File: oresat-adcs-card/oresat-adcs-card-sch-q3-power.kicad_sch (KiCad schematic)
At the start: 86 parts, among them Q31 MOSFET-PCH-SOT23-6, Q32 MOSFET-PCH-SOT23-6, Q33 PMV45EN2R, Q34 PMV45EN2R, U25 MAX7310ATE, U26 MAX4211FETE, U27 MIC842LYC5-TR, U28 MIC842LYC5-TR

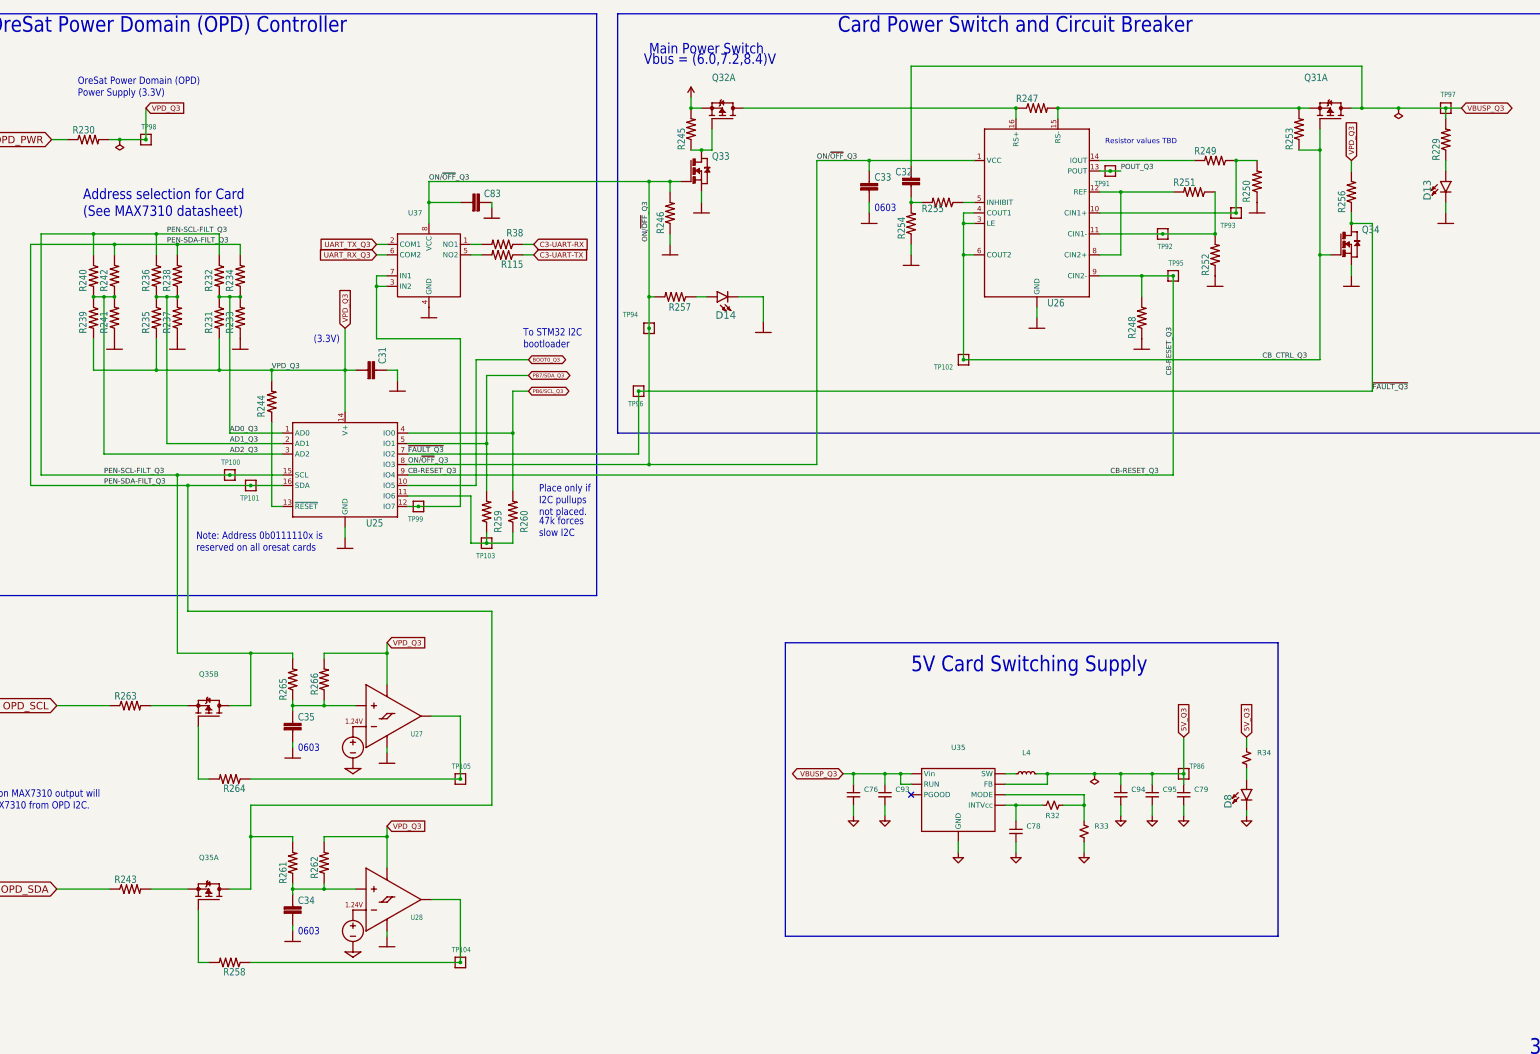
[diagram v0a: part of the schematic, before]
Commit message: Design review changes
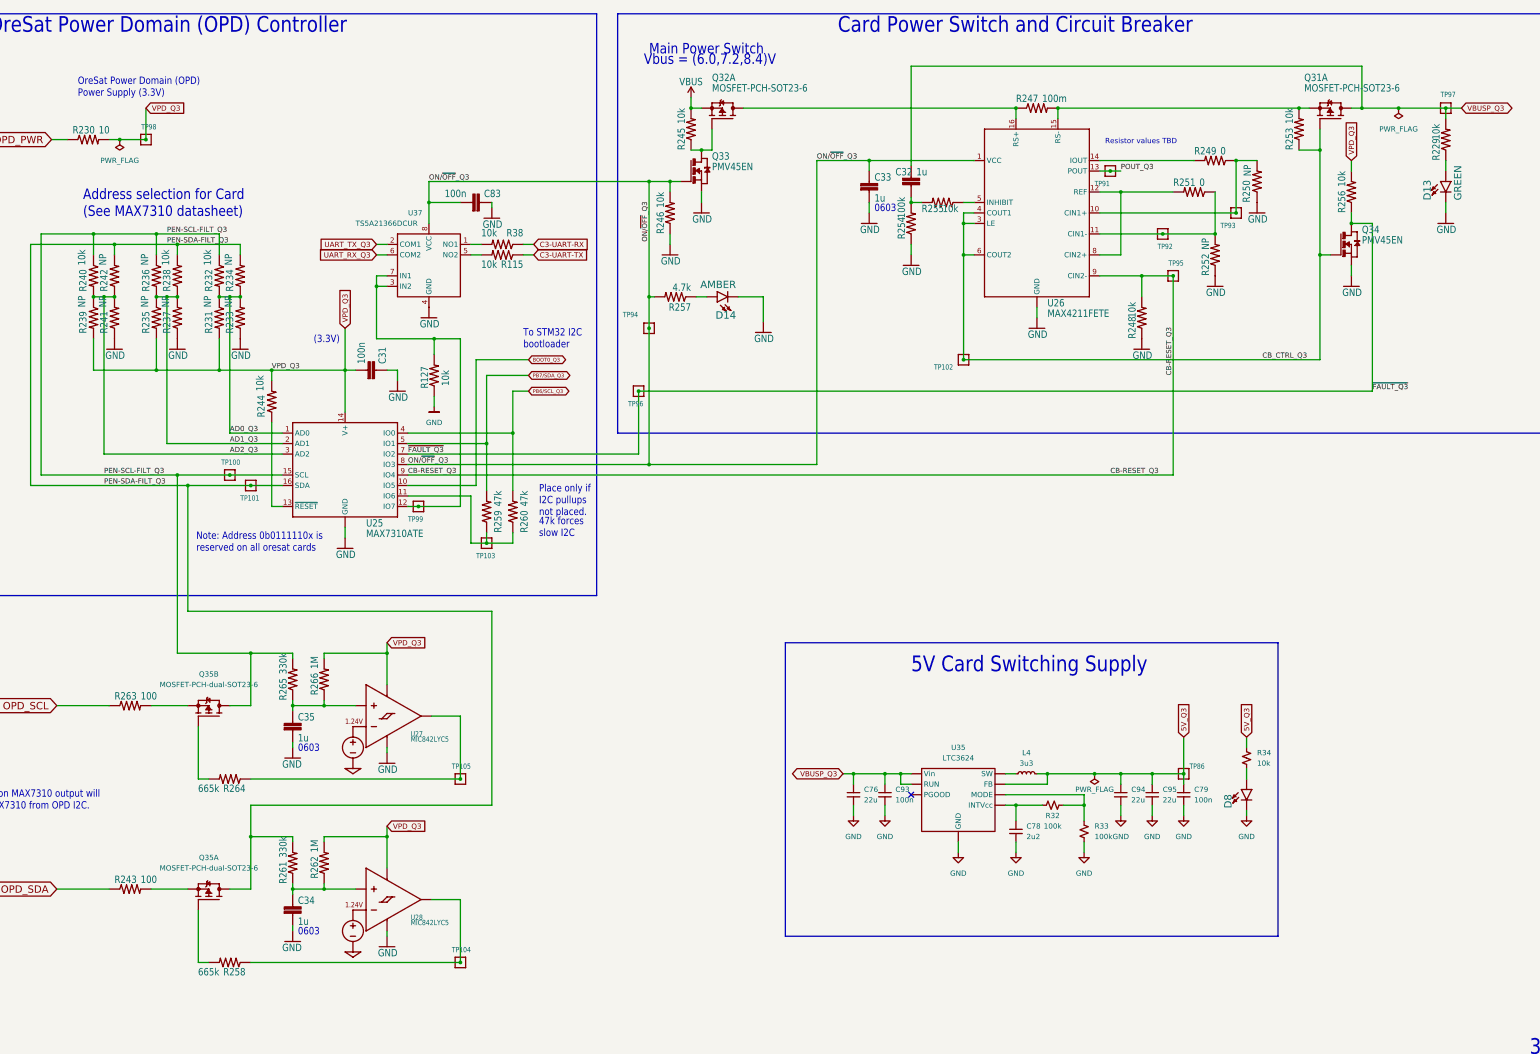
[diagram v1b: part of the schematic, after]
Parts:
- added R127: CRGCQ0603F2K7, oresat-acs-card:.0603-C-NOSILK, symbol oresat-acs-card-eagle-import:R-US_0603-C-NOSILK
- C31, C33, C34, C35, C83, R115, R229, R230, R231, R232, R233, R234, R235, R236, R237, R238, R239, R240, R241, R242, R243, R244, R245, R246, R248, R249, R250, R251, R252, R253, R254, R255, R256, R257, R258, R259, R260, R261, R262, R263, R264, R265, R266, R38: footprint (none) -> oresat-acs-card:.0603-C-NOSILK
- C32: value (none) -> 1u; footprint (none) -> oresat-acs-card:.0603-C-NOSILK
- C76, C94, C95: value (none) -> 22u; footprint (none) -> Capacitor_SMD:C_1210_3225Metric
- C78: value (none) -> 2u2; footprint (none) -> Capacitor_SMD:C_0603_1608Metric
- C79, C93: value (none) -> 100n; footprint (none) -> Capacitor_SMD:C_0603_1608Metric
- D13, D14, D8: footprint (none) -> oresat-acs-card:LED-0603
- L4: value (none) -> 3u3; footprint (none) -> Inductor_SMD:L_Coilcraft_XxL4030
- Q31, Q32: footprint (none) -> oresat-acs-card:SOT23-6
- Q33, Q34: footprint (none) -> oresat-acs-card:SOT23
- Q35: value (none) -> MOSFET-PCH-dual-SOT23-6; footprint (none) -> oresat-acs-card:SOT23-6
- R247: footprint (none) -> oresat-acs-card:R1206
- R32, R33: value (none) -> 100k; footprint (none) -> Resistor_SMD:R_0603_1608Metric
- R34: value (none) -> 10k; footprint (none) -> Resistor_SMD:R_0603_1608Metric
- TP100, TP101, TP102, TP103, TP104, TP105, TP86, TP91, TP92, TP93, TP94, TP95, TP96, TP97, TP98, TP99: value (none) -> TEST-POINT-LARGE-SQUARE; footprint (none) -> oresat-acs-card:1X01
- U25, U26: footprint (none) -> oresat-acs-card:QFN65P400X400X80-17T210
- U27, U28: footprint (none) -> oresat-acs-card:SC70-5
- U35: value (none) -> LTC3624; footprint (none) -> oresat-footprints:DFN-8-1EP_3x3mm_P0.5mm_EP1.65x2.38mm_ThermalVias0.3mm
- U37: value (none) -> TS5A21366DCUR; footprint (none) -> oresat-acs-card:DCU-R-PDSO-G8
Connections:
- net GND: now also R127.1
- net at TP99.1, U25.12 (IO7), U37.3 (IN2)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: now also R127.2

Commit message: Updated inductor footprint
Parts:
- L4: footprint Inductor_SMD:L_Coilcraft_XxL4030 -> oresat-footprints:L_ECS-MPI4040
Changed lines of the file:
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@@
     (property "Reference" "L4" (id 0) (at 285.75 193.04 90))
     (property "Value" "3u3" (id 1) (at 285.75 195.58 90))
-    (property "Footprint" "Inductor_SMD:L_Coilcraft_XxL4030" (id 2) (at 285.75 198.12 0)
+    (property "Footprint" "oresat-footprints:L_ECS-MPI4040" (id 2) (at 285.75 198.12 0)
       (effects (font (size 1.27 1.27)) hide)
     )

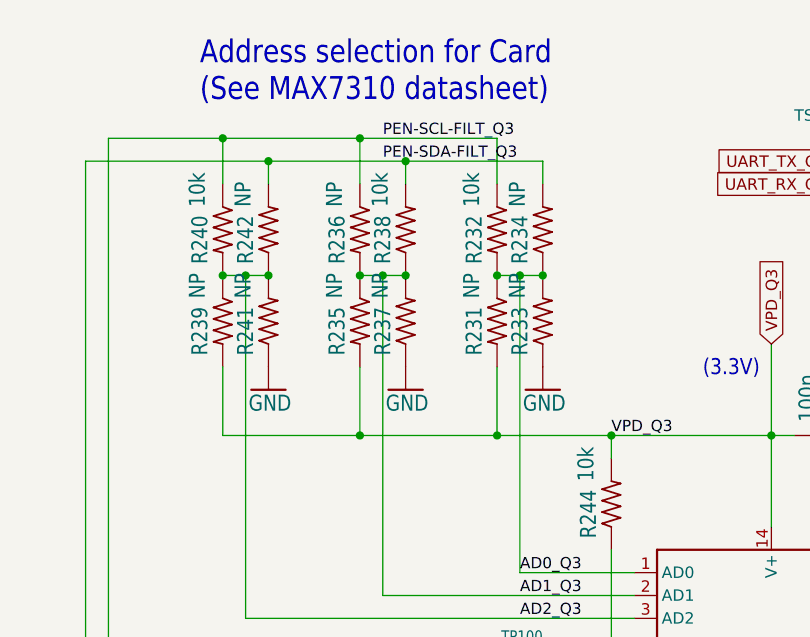
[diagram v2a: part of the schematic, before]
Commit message: Updated MT OPD breaker current limiting, and added OPD addresses to schematic
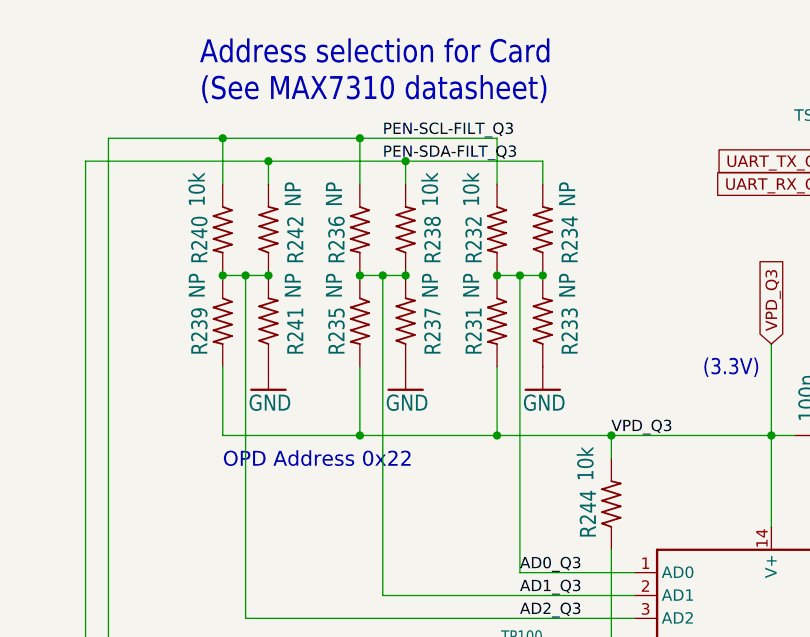
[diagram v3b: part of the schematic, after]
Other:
- note added: "OPD Address 0x22"
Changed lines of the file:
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@@
     (effects (font (size 1.778 1.5113)) (justify left bottom))
+  )
+  (text "OPD Address 0x22" (at 59.69 104.14 0)
+    (effects (font (size 1.651 1.651)) (justify left bottom))
   )
   (text "0603" (at 109.22 193.04 180)
@@
   (symbol (lib_id "oresat-acs-card-eagle-import:R-US_0603-C-NOSILK") (at 64.77 77.47 90) (unit 1)
     (in_bom yes) (on_board yes)
-    (property "Reference" "R242" (id 0) (at 63.2714 81.28 0)
-      (effects (font (size 1.778 1.5113)) (justify left bottom))
-    )
-    (property "Value" "NP" (id 1) (at 62.992 74.93 0)
+    (property "Reference" "R242" (id 0) (at 68.8594 81.28 0)
+      (effects (font (size 1.778 1.5113)) (justify left bottom))
+    )
+    (property "Value" "NP" (id 1) (at 68.58 74.93 0)
       (effects (font (size 1.778 1.5113)) (justify left bottom))
     )
@@
   (symbol (lib_id "oresat-acs-card-eagle-import:R-US_0603-C-NOSILK") (at 95.25 77.47 90) (unit 1)
     (in_bom yes) (on_board yes)
-    (property "Reference" "R234" (id 0) (at 93.7514 81.28 0)
-      (effects (font (size 1.778 1.5113)) (justify left bottom))
-    )
-    (property "Value" "NP" (id 1) (at 93.472 74.93 0)
+    (property "Reference" "R234" (id 0) (at 99.3394 81.28 0)
+      (effects (font (size 1.778 1.5113)) (justify left bottom))
+    )
+    (property "Value" "NP" (id 1) (at 99.06 74.93 0)
       (effects (font (size 1.778 1.5113)) (justify left bottom))
     )
@@
   (symbol (lib_id "oresat-acs-card-eagle-import:R-US_0603-C-NOSILK") (at 80.01 87.63 90) (unit 1)
     (in_bom yes) (on_board yes)
-    (property "Reference" "R237" (id 0) (at 78.5114 91.44 0)
-      (effects (font (size 1.778 1.5113)) (justify left bottom))
-    )
-    (property "Value" "NP" (id 1) (at 78.232 85.09 0)
+    (property "Reference" "R237" (id 0) (at 84.0994 91.44 0)
+      (effects (font (size 1.778 1.5113)) (justify left bottom))
+    )
+    (property "Value" "NP" (id 1) (at 83.82 85.09 0)
       (effects (font (size 1.778 1.5113)) (justify left bottom))
     )
@@
   (symbol (lib_id "oresat-acs-card-eagle-import:R-US_0603-C-NOSILK") (at 64.77 87.63 90) (unit 1)
     (in_bom yes) (on_board yes)
-    (property "Reference" "R241" (id 0) (at 63.2714 91.44 0)
-      (effects (font (size 1.778 1.5113)) (justify left bottom))
-    )
-    (property "Value" "NP" (id 1) (at 62.992 85.09 0)
+    (property "Reference" "R241" (id 0) (at 68.8594 91.44 0)
+      (effects (font (size 1.778 1.5113)) (justify left bottom))
+    )
+    (property "Value" "NP" (id 1) (at 68.58 85.09 0)
       (effects (font (size 1.778 1.5113)) (justify left bottom))
     )
@@
   (symbol (lib_id "oresat-acs-card-eagle-import:R-US_0603-C-NOSILK") (at 95.25 87.63 90) (unit 1)
     (in_bom yes) (on_board yes)
-    (property "Reference" "R233" (id 0) (at 93.7514 91.44 0)
-      (effects (font (size 1.778 1.5113)) (justify left bottom))
-    )
-    (property "Value" "NP" (id 1) (at 93.472 85.09 0)
+    (property "Reference" "R233" (id 0) (at 99.3394 91.44 0)
+      (effects (font (size 1.778 1.5113)) (justify left bottom))
+    )
+    (property "Value" "NP" (id 1) (at 99.06 85.09 0)
       (effects (font (size 1.778 1.5113)) (justify left bottom))
     )
@@
   (symbol (lib_id "oresat-acs-card-eagle-import:R-US_0603-C-NOSILK") (at 80.01 77.47 90) (unit 1)
     (in_bom yes) (on_board yes)
-    (property "Reference" "R238" (id 0) (at 78.5114 81.28 0)
-      (effects (font (size 1.778 1.5113)) (justify left bottom))
-    )
-    (property "Value" "10k" (id 1) (at 78.232 74.93 0)
-      (effects (font (size 1.778 1.5113)) (justify left bottom))
-    )
+    (property "Reference" "R238" (id 0) (at 84.0994 81.28 0)
+      (effects (font (size 1.778 1.5113)) (justify left bottom))
+    )
+    (property "Value" "10k" (id 1) (at 83.82 74.93 0)
+      (effects (font (size 1.778 1.5113)) (justify left bottom))
+    )

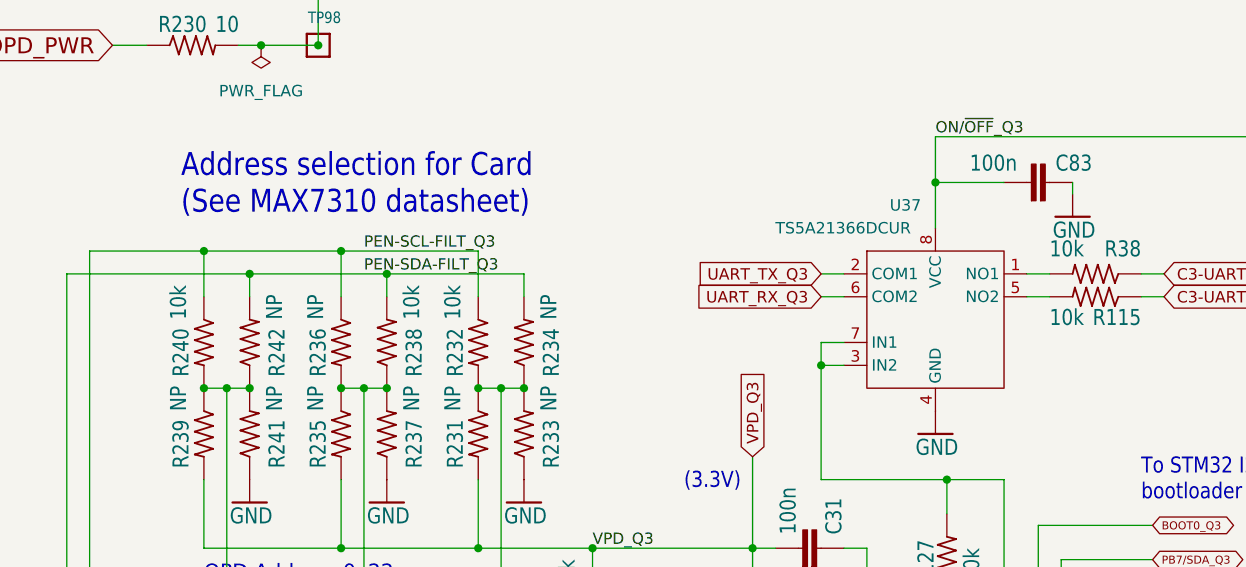
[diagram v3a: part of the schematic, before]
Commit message: Fixed ADCS card issues
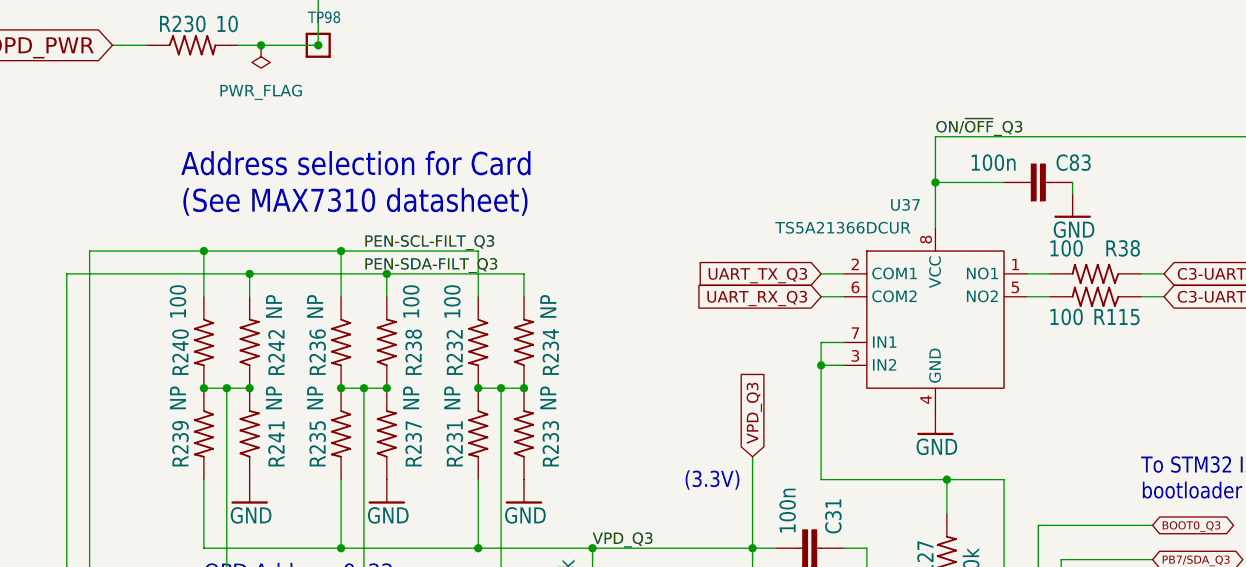
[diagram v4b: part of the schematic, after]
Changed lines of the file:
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@@
       (effects (font (size 1.778 1.5113)) (justify left bottom))
     )
-    (property "Value" "10k" (id 1) (at 157.48 73.66 0)
+    (property "Value" "100" (id 1) (at 157.48 73.66 0)
       (effects (font (size 1.778 1.5113)) (justify left bottom))
     )
@@
       (effects (font (size 1.778 1.5113)) (justify left bottom))
     )
-    (property "Value" "10k" (id 1) (at 157.48 66.04 0)
+    (property "Value" "100" (id 1) (at 157.48 66.04 0)
       (effects (font (size 1.778 1.5113)) (justify left bottom))
     )
@@
       (effects (font (size 1.778 1.5113)) (justify left bottom))
     )
-    (property "Value" "10k" (id 1) (at 83.82 74.93 0)
+    (property "Value" "100" (id 1) (at 83.82 74.93 0)
       (effects (font (size 1.778 1.5113)) (justify left bottom))
     )
@@
       (effects (font (size 1.778 1.5113)) (justify right top))
     )
-    (property "Value" "10k" (id 1) (at 88.392 74.93 0)
+    (property "Value" "100" (id 1) (at 88.392 74.93 0)
       (effects (font (size 1.778 1.5113)) (justify right top))
     )
@@
       (effects (font (size 1.778 1.5113)) (justify right top))
     )
-    (property "Value" "10k" (id 1) (at 57.912 74.93 0)
+    (property "Value" "100" (id 1) (at 57.912 74.93 0)
       (effects (font (size 1.778 1.5113)) (justify right top))
     )

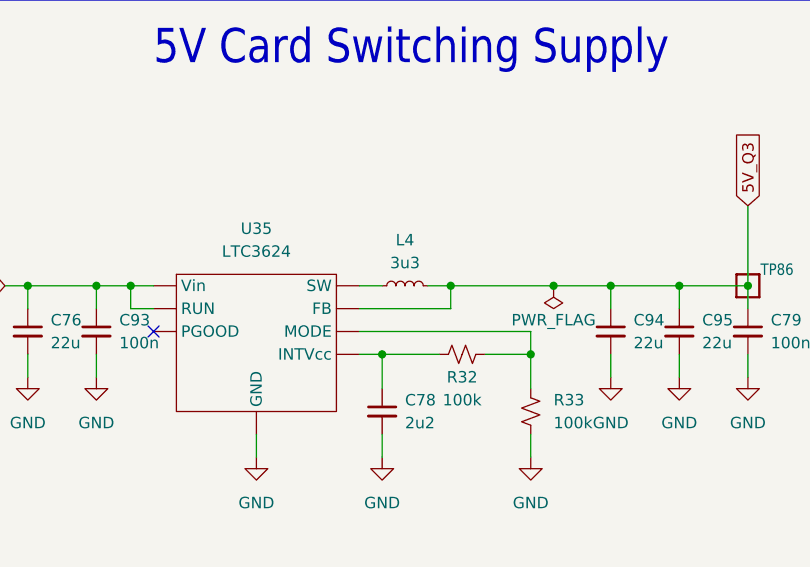
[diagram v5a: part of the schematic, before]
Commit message: Changed MT current limit setting, and added filter for current sense to ADC
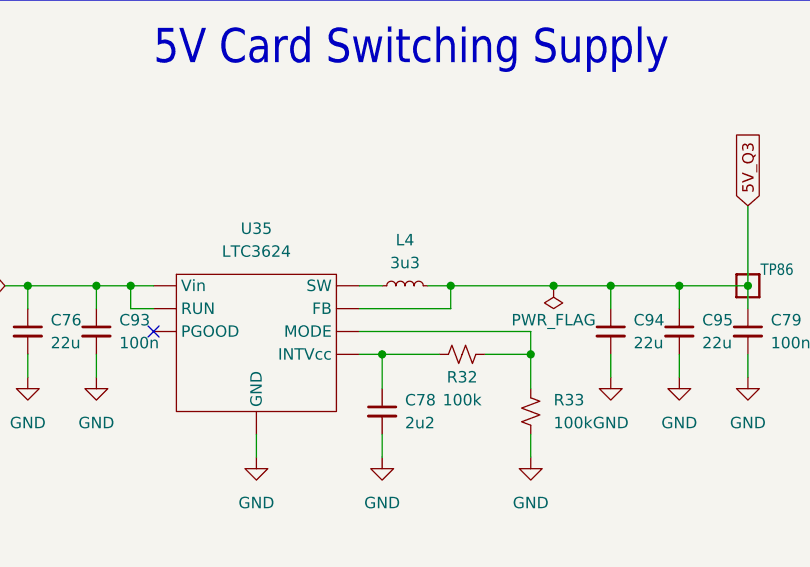
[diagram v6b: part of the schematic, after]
